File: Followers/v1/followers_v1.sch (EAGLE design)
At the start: 105 parts, among them IC1 OPA1641, IC14 TL072D, IC2 LM324PW, IC3 LM324PW, IC4 LM324PW, IC5 LM324PW, IC6 LM4040B10, IC7 LM324PW, IC8 LM324PW, IC9 LM324PW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

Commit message: Clean up power section
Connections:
- net !GATE: no longer IC9B.OUT
- net ENVELOPE: no longer IC9B.-IN
- net GATE: no longer IC9A.OUT
- net GND: no longer IC9A.+IN
- net N$1: no longer IC9B.+IN
- net N$8: no longer IC9A.-IN
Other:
- note added: "MISSING OPAMPS AND IC PARTS DO INVOKE"

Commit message: Fixed op-amps
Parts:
- removed D3: DNP, diode:DIODE_2CACA-SOT23
- removed IC14: TL072D, og-linear:TL072D
- removed IC5, IC7, IC8: LM324PW, og-ics:LM324PW
- added C17: 4.7u, rcl:C-USC0603
- added C18: 100n, rcl:C-USC0402
- IC4: value LM324PW -> TL072D; device og-ics:LM324PW -> og-linear:TL072D
- R7: value 50kB -> 50k
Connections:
- removed net ENVELOPE: IC7A.-IN, IC7A.OUT
- new net N$27: C17.1, J6.3
- new net N$32: C17.2, IC2A.+IN
- net AREF_+10: now also IC2D.-IN; no longer IC5C.-IN
- net FULL_WAVE_RECT: now also IC2C.OUT, IC2D.+IN; no longer IC4D.OUT, IC5C.+IN
- net FWR_CLIP: now also IC2D.OUT; no longer IC5C.OUT
- net GND: now also C18.1, C4.1, C6.2, IC4P.V-; no longer C4.2, C6.1, IC14P.V-, IC2P.V-
- net N$100: now also IC4A.OUT; no longer IC14A.OUT
- net N$101: now also IC4B.OUT; no longer IC14B.OUT
- net N$11: now also IC2B.-IN; no longer IC4C.-IN
- net N$12: now also IC2C.+IN; no longer IC4D.+IN
- net N$14: now also IC2C.-IN; no longer IC4D.-IN
- net N$17: now also IC3D.-IN; no longer IC8B.-IN
- net N$19: no longer IC7A.+IN
- net N$2: no longer D3.AC
- net N$30: now also IC3D.OUT; no longer IC8B.OUT
- net N$33: now also IC2A.-IN, IC2A.OUT, IC2B.+IN; no longer IC4C.+IN, J6.3
- net N$5: now also IC2B.OUT; no longer IC4C.OUT
- net N$96: now also IC4A.+IN, IC4B.-IN; no longer IC14A.+IN, IC14B.-IN
- net N$97: now also IC4A.-IN; no longer IC14A.-IN
- net N$99: now also IC4B.+IN; no longer IC14B.+IN
- net SLEW: now also IC3D.+IN; no longer IC8B.+IN
- net VCC: now also C6.1, IC4P.V+; no longer C4.1, D3.C, IC14P.V+
- net VEE: now also C18.2, C4.2, IC2P.V-; no longer C6.2, D3.A
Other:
- note added: "https://kassu2000.blogspot.com/2016/04/slope-generator.html https://everycircuit.com/circuit/5797591789600768"
- note added: "https://www.ti.com/lit/ug/tidu030/tidu030.pdf https://everycircuit.com/circuit/4720296081489920"
- note removed: "BAT54S"
- note removed: "https://kassu2000.blogspot.com/2016/04/slope-generator.html"
- moved on the sheet: C12, C13, C15, C16, C4, C6, C7, C8, C9, D4, D7, D8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

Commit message: Slew rate limiter
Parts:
- removed JP1, JP3: (no value), SparkFun:M03PTH
- removed R24: 10k, rcl:R-US_R0402
- removed R27: 1.0M, rcl:R-US_R0402
- added J11, J4: PJ301_THONKICONN6, og-pj301:PJ301_THONKICONN6
- added R18, R19: 50k, og-pots:POT_USVERTICAL_PS
- C11: value 1u -> 10u
- R23: value 100k -> 510
- R25: value 2.7k -> 100k
- R26: value 20k -> 47k
- R28: value 430k -> 47k
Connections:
- new net LP_DC: J11.2, R23.1
- new net N$40: J4.3, R23.2
- new net N$41: J11.3
- new net N$42: J10.3
- net FULL_WAVE_RECT: no longer D5.A, D6.C
- net GND: now also IC3A.+IN, IC3B.-IN, IC3C.+IN, J11.1, J4.1; no longer C11.2, R27.1
- net N$18: now also IC3A.-IN, R25.2; no longer D5.C, JP1.2
- net N$19: now also IC3A.OUT, R26.1; no longer C11.1, R23.2, R24.2, R25.2, R26.2, R27.2, R28.2
- net N$21: now also IC3B.+IN, R26.2, R28.1; no longer JP3.3, R24.1
- net N$23: now also D5.A, D6.C, IC3B.OUT; no longer JP3.1, R23.1
- net N$24: now also D5.C, R19.A; no longer D6.A, JP3.2, R28.1
- net N$25: now also D6.A, R18.A; no longer JP1.1, R25.1
- net N$26: now also C11.1, IC3C.-IN, R18.S, R19.S; no longer JP1.3, R26.1
- net N$29: now also R25.1
- net SLEW: now also C11.2, IC3C.OUT, R28.2
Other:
- note added: "DC Matching LP Filter"
- note added: "bipolar op-amp, 0-5v output"
- note added: "bipolar op-amps only"
- note removed: "Attack time"
- note removed: "Classic envelope follower R-C topology."
- note removed: "Decay time"
- note removed: "Envelope Follower"
- note removed: "MISSING OPAMPS AND IC PARTS DO INVOKE"
- note removed: "Output buffer."
- note removed: "Seperate resistor for each direction. Switchable."

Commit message: bomf
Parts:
- removed JP2: (no value), SparkFun:M03PTH
- removed R12, R20, R21: 100k, rcl:R-US_R0402
- removed R13, R14, R15, R16, R17: 200k, rcl:R-US_R0402
- removed R22: 20k, rcl:R-US_R0402
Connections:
- removed net !GATE: R15.1, R17.2
- removed net GATE: C10.2, R14.2
- removed net N$1: JP2.2, R16.2, R17.1, R21.1
- removed net N$35: JP2.1, R22.1
- removed net N$36: JP2.3, R20.1
- removed net N$39: R12.1, R13.1
- removed net N$8: C10.1, R13.2, R14.1, R15.2
- net GND: no longer R20.2, R21.2, R22.2
- net VCC: no longer R16.1
- net VEE: no longer R12.2
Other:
- note removed: "Gate Detector"
- note removed: "Switchable Resistor"
- moved on the sheet: C10

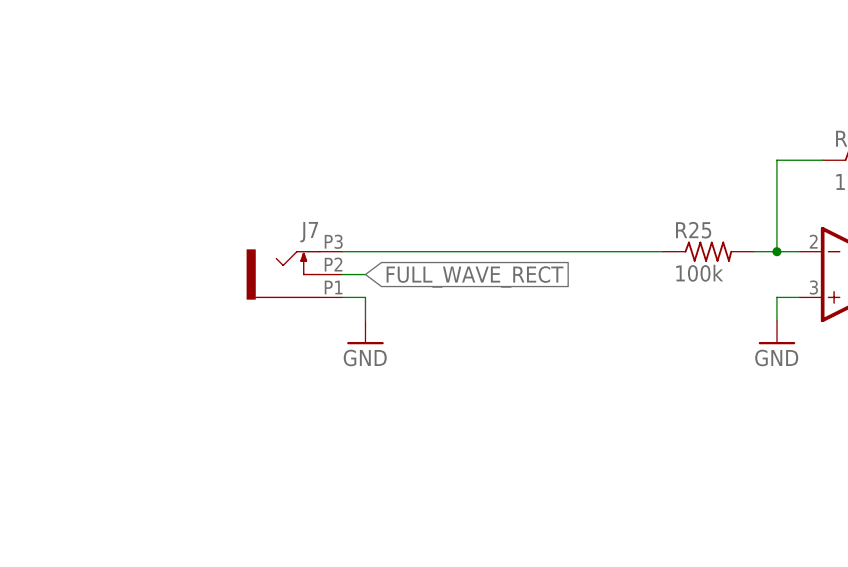
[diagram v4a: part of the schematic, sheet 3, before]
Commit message: Input resistor
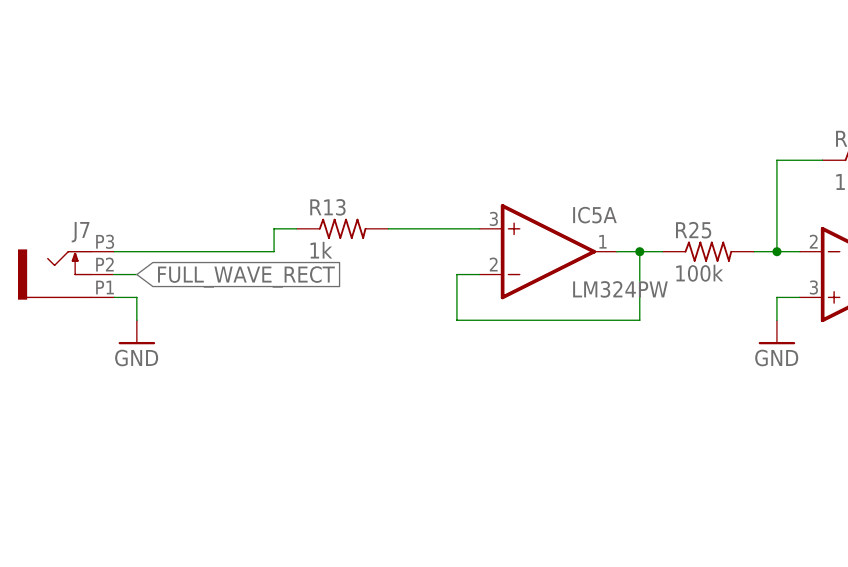
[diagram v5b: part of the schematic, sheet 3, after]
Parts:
- added C19, C20: 100n, rcl:C-USC0402
- added IC5: LM324PW, og-ics:LM324PW
- added R12: 50k, og-pots:POT_USVERTICAL_PS
- added R13: 1k, rcl:R-US_R0402
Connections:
- new net N$1: J7.3, R13.1
- new net N$8: IC5A.-IN, IC5A.OUT, R25.1
- net GND: now also C19.2, C20.1
- net N$29: now also IC5A.+IN, R13.2; no longer J7.3, R25.1
- net VCC: now also C19.1, IC5P.V+
- net VEE: now also C20.2, IC5P.V-
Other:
- note added: "Lowpass Filter"
- note removed: "DC Matching LP Filter"
- moved on the sheet: J7
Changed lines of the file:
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@@
 <part name="P+2" library="SparkFun" deviceset="VCC" device=""/>
 <part name="C10" library="rcl" deviceset="C-US" device="C0402" value="68p"/>
+<part name="R12" library="og-pots" deviceset="POT_US" device="VERTICAL_PS" value="50k"/>
+<part name="IC5" library="og-ics" deviceset="LM324" device="PW"/>
+<part name="GND11" library="SparkFun" deviceset="GND" device=""/>
+<part name="P+9" library="SparkFun" deviceset="VCC" device=""/>
+<part name="SUPPLY6" library="supply2" deviceset="VEE" device=""/>
+<part name="C19" library="rcl" deviceset="C-US" device="C0402" value="100n"/>
+<part name="C20" library="rcl" deviceset="C-US" device="C0402" value="100n"/>
+<part name="R13" library="rcl" deviceset="R-US_" device="R0402" value="1k"/>
 </parts>
 <sheets>
@@
 <attribute name="SHEET" x="230.505" y="5.08" size="2.54" layer="94" font="vector"/>
 </instance>
-<instance part="GND22" gate="1" x="45.72" y="86.36" smashed="yes">
-<attribute name="VALUE" x="43.18" y="83.82" size="1.778" layer="96"/>
-</instance>
-<instance part="J7" gate="G$1" x="38.1" y="93.98" smashed="yes" rot="MR0">
-<attribute name="NAME" x="40.64" y="98.044" size="1.778" layer="95" rot="MR0"/>
+<instance part="GND22" gate="1" x="20.32" y="86.36" smashed="yes">
+<attribute name="VALUE" x="17.78" y="83.82" size="1.778" layer="96"/>
+</instance>
+<instance part="J7" gate="G$1" x="12.7" y="93.98" smashed="yes" rot="MR0">
+<attribute name="NAME" x="15.24" y="98.044" size="1.778" layer="95" rot="MR0"/>
 </instance>
 <instance part="GND15" gate="1" x="215.9" y="86.36" smashed="yes" rot="MR0">
@@
 <instance part="GND28" gate="1" x="177.8" y="88.9" smashed="yes">
 <attribute name="VALUE" x="175.26" y="86.36" size="1.778" layer="96"/>
+</instance>
+<instance part="IC5" gate="A" x="66.04" y="96.52" smashed="yes">
+<attribute name="NAME" x="68.58" y="99.695" size="1.778" layer="95"/>
+<attribute name="VALUE" x="68.58" y="91.44" size="1.778" layer="96"/>
+</instance>
+<instance part="R13" gate="G$1" x="43.18" y="99.06" smashed="yes">
+<attribute name="NAME" x="39.37" y="100.5586" size="1.778" layer="95"/>
+<attribute name="VALUE" x="39.37" y="95.758" size="1.778" layer="96"/>
 </instance>
 </instances>
@@
 <segment>
 <pinref part="GND22" gate="1" pin="GND"/>
-<wire x1="45.72" y1="88.9" x2="45.72" y2="91.44" width="0.1524" layer="91"/>
+<wire x1="20.32" y1="88.9" x2="20.32" y2="91.44" width="0.1524" layer="91"/>
 <pinref part="J7" gate="G$1" pin="1"/>
-<wire x1="45.72" y1="91.44" x2="43.18" y2="91.44" width="0.1524" layer="91"/>
+<wire x1="20.32" y1="91.44" x2="17.78" y2="91.44" width="0.1524" layer="91"/>
 </segment>
 <segment>
@@
 <segment>
 <pinref part="J7" gate="G$1" pin="2"/>
-<wire x1="43.18" y1="93.98" x2="45.72" y2="93.98" width="0.1524" layer="91"/>
-<label x="45.72" y="93.98" size="1.778" layer="95" xref="yes"/>
-</segment>
-</net>
-<net name="N$29" class="0">
-<segment>
-<pinref part="J7" gate="G$1" pin="3"/>
-<wire x1="43.18" y1="96.52" x2="78.74" y2="96.52" width="0.1524" layer="91"/>
-<pinref part="R25" gate="G$1" pin="1"/>
+<wire x1="17.78" y1="93.98" x2="20.32" y2="93.98" width="0.1524" layer="91"/>
+<label x="20.32" y="93.98" size="1.778" layer="95" xref="yes"/>
 </segment>
 </net>
@@
 </segment>
 </net>
+<net name="N$8" class="0">
+<segment>
+<pinref part="IC5" gate="A" pin="-IN"/>
+<wire x1="58.42" y1="93.98" x2="55.88" y2="93.98" width="0.1524" layer="91"/>
+<wire x1="55.88" y1="93.98" x2="55.88" y2="88.9" width="0.1524" layer="91"/>
+<wire x1="55.88" y1="88.9" x2="76.2" y2="88.9" width="0.1524" layer="91"/>
+<wire x1="76.2" y1="88.9" x2="76.2" y2="96.52" width="0.1524" layer="91"/>
+<pinref part="IC5" gate="A" pin="OUT"/>
+<wire x1="76.2" y1="96.52" x2="73.66" y2="96.52" width="0.1524" layer="91"/>
+<pinref part="R25" gate="G$1" pin="1"/>
+<wire x1="78.74" y1="96.52" x2="76.2" y2="96.52" width="0.1524" layer="91"/>
+<junction x="76.2" y="96.52"/>
+</segment>
+</net>
+<net name="N$1" class="0">
+<segment>
+<pinref part="J7" gate="G$1" pin="3"/>
+<wire x1="17.78" y1="96.52" x2="35.56" y2="96.52" width="0.1524" layer="91"/>
+<wire x1="35.56" y1="96.52" x2="35.56" y2="99.06" width="0.1524" layer="91"/>
+<pinref part="R13" gate="G$1" pin="1"/>
+<wire x1="35.56" y1="99.06" x2="38.1" y2="99.06" width="0.1524" layer="91"/>
+</segment>
+</net>
+<net name="N$29" class="0">
+<segment>
+<pinref part="R13" gate="G$1" pin="2"/>
+<pinref part="IC5" gate="A" pin="+IN"/>
+<wire x1="48.26" y1="99.06" x2="58.42" y2="99.06" width="0.1524" layer="91"/>
+</segment>
+</net>
 </nets>
 </sheet>
 <sheet>
-<description>DC Matching LP Filter</description>
+<description>Lowpass Filter</description>
 <plain>
 <text x="162.56" y="20.32" size="2.54" layer="94">cc-by-sa</text>
-<text x="215.9" y="20.32" size="2.54" layer="94">DC Matching LP Filter</text>
+<text x="215.9" y="20.32" size="2.54" layer="94">Lowpass Filter</text>
 <text x="162.56" y="15.24" size="2.54" layer="94">Ella Jameson</text>
 <text x="162.56" y="10.16" size="2.54" layer="94">ellagjameson@gmail.com</text>
@@
 <attribute name="NAME" x="212.09" y="95.4786" size="1.778" layer="95"/>
 <attribute name="VALUE" x="212.09" y="90.678" size="1.778" layer="96"/>
+</instance>
+<instance part="R12" gate="G$1" x="93.98" y="106.68" smashed="yes" rot="R270">
+<attribute name="NAME" x="91.44" y="111.76" size="1.778" layer="95"/>
+<attribute name="VALUE" x="91.44" y="109.22" size="1.778" layer="96"/>
+</instance>
+<instance part="IC5" gate="D" x="114.3" y="162.56" smashed="yes" rot="MR180">
+<attribute name="NAME" x="116.84" y="159.385" size="1.778" layer="95" rot="MR180"/>
+<attribute name="VALUE" x="116.84" y="167.64" size="1.778" layer="96" rot="MR180"/>
+</instance>
+<instance part="IC5" gate="C" x="142.24" y="162.56" smashed="yes">
+<attribute name="NAME" x="144.78" y="165.735" size="1.778" layer="95"/>
+<attribute name="VALUE" x="144.78" y="157.48" size="1.778" layer="96"/>
+</instance>
+<instance part="IC5" gate="B" x="170.18" y="160.02" smashed="yes">
+<attribute name="NAME" x="172.72" y="163.195" size="1.778" layer="95"/>
+<attribute name="VALUE" x="172.72" y="154.94" size="1.778" layer="96"/>
 </instance>
 </instances>
@@
 <instance part="SUPPLY5" gate="G$1" x="185.42" y="88.9" smashed="yes" rot="R180">
 <attribute name="VALUE" x="187.325" y="85.725" size="1.778" layer="96" rot="R180"/>
+</instance>
+<instance part="IC5" gate="P" x="236.22" y="106.68" smashed="yes"/>
+<instance part="GND11" gate="1" x="218.44" y="101.6" smashed="yes">
+<attribute name="VALUE" x="215.9" y="99.06" size="1.778" layer="96"/>
+</instance>
+<instance part="P+9" gate="1" x="236.22" y="121.92" smashed="yes">
+<attribute name="VALUE" x="235.204" y="125.476" size="1.778" layer="96"/>
+</instance>
+<instance part="SUPPLY6" gate="G$1" x="236.22" y="88.9" smashed="yes" rot="R180">
+<attribute name="VALUE" x="238.125" y="85.725" size="1.778" layer="96" rot="R180"/>
+</instance>
+<instance part="C19" gate="G$1" x="226.06" y="114.3" smashed="yes">
+<attribute name="NAME" x="227.076" y="114.935" size="1.778" layer="95"/>
+<attribute name="VALUE" x="227.076" y="110.109" size="1.778" layer="96"/>
+</instance>
+<instance part="C20" gate="G$1" x="226.06" y="101.6" smashed="yes">
+<attribute name="NAME" x="227.076" y="102.235" size="1.778" layer="95"/>
+<attribute name="VALUE" x="227.076" y="97.409" size="1.778" layer="96"/>
 </instance>
 </instances>
@@
 <junction x="175.26" y="106.68"/>
 </segment>
+<segment>
+<wire x1="218.44" y1="106.68" x2="218.44" y2="104.14" width="0.1524" layer="91"/>
+<wire x1="226.06" y1="109.22" x2="226.06" y2="106.68" width="0.1524" layer="91"/>
+<wire x1="226.06" y1="104.14" x2="226.06" y2="106.68" width="0.1524" layer="91"/>
+<junction x="226.06" y="106.68"/>
+<wire x1="226.06" y1="106.68" x2="218.44" y2="106.68" width="0.1524" layer="91"/>
+<pinref part="GND11" gate="1" pin="GND"/>
+<pinref part="C19" gate="G$1" pin="2"/>
+<pinref part="C20" gate="G$1" pin="1"/>
+</segment>
 </net>
 <net name="VEE" class="0">
@@
 <junction x="185.42" y="93.98"/>
 </segment>
+<segment>
+<wire x1="236.22" y1="99.06" x2="236.22" y2="93.98" width="0.1524" layer="91"/>
+<wire x1="236.22" y1="91.44" x2="236.22" y2="93.98" width="0.1524" layer="91"/>
+<wire x1="226.06" y1="96.52" x2="226.06" y2="93.98" width="0.1524" layer="91"/>
+<junction x="236.22" y="93.98"/>
+<wire x1="226.06" y1="93.98" x2="236.22" y2="93.98" width="0.1524" layer="91"/>
+<junction x="236.22" y="93.98"/>
+<pinref part="IC5" gate="P" pin="V-"/>
+<pinref part="SUPPLY6" gate="G$1" pin="VEE"/>
+<pinref part="C20" gate="G$1" pin="2"/>
+</segment>
 </net>
 <net name="VCC" class="0">
@@
 <junction x="185.42" y="119.38"/>
 </segment>
-</net>
+<segment>
+<wire x1="236.22" y1="114.3" x2="236.22" y2="119.38" width="0.1524" layer="91"/>
+<wire x1="236.22" y1="121.92" x2="236.22" y2="119.38" width="0.1524" layer="91"/>
+<wire x1="226.06" y1="119.38" x2="236.22" y2="119.38" width="0.1524" layer="91"/>
+<wire x1="226.06" y1="116.84" x2="226.06" y2="119.38" width="0.1524" layer="91"/>
+<junction x="236.22" y="119.38"/>
+<junction x="236.22" y="119.38"/>
+<pinref part="IC5" gate="P" pin="V+"/>
+<pinref part="P+9" gate="1" pin="VCC"/>
+<pinref part="C19" gate="G$1" pin="1"/>
+</segment>
+</net>

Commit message: Filter
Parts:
- removed IC9: LM324PW, og-ics:LM324PW
- added C21: TBD, rcl:C-USC0402
- added R14, R15, R16: 1k, rcl:R-US_R0402
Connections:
- removed net LP_DC: J11.2, R23.1
- new net LOWPASS: IC5C.-IN, IC5C.OUT, J11.2, R23.1
- new net N$35: C21.1, IC5C.+IN, R12.A
- new net N$36: IC5B.+IN, R14.2
- new net N$39: J8.3, R14.1
- new net N$43: IC5B.-IN, IC5B.OUT, R12.S
- new net N$45: R16.2
- net COMP: now also IC5D.+IN; no longer IC9D.+IN
- net GND: now also C21.2
- net N$17: now also IC5A.-IN; no longer IC3D.-IN
- net N$29: now also IC3D.+IN; no longer IC5A.+IN
- net N$30: now also IC5A.OUT; no longer IC3D.OUT
- net N$37: now also IC5D.-IN; no longer IC9D.-IN
- net N$38: now also IC5D.OUT; no longer IC9D.OUT
- net N$41: now also R15.1
- net N$42: now also R16.1
- net N$8: now also IC3D.-IN, IC3D.OUT; no longer IC5A.-IN, IC5A.OUT
- net SLEW: now also IC5A.+IN; no longer IC3D.+IN
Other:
- note added: "FIND VAL"
- note removed: "bipolar op-amps only"
- moved on the sheet: C11, D5, D6, IC3A, IC3B, IC3C, IC3D, IC5A, IC5B, IC5C, J3, J4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
